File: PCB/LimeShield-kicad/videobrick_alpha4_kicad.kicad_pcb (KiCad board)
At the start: 4 copper layers, 53.2 x 59.6 mm, 91 parts, among them K1 WE-685119134923, Q1 BSS123, Q2 BSS123, Q3 BSS123, Q4 BSS123, U1 ADV7611BSWZ-P, U2 TPS720xx, Y1 CRYSTAL_SMD

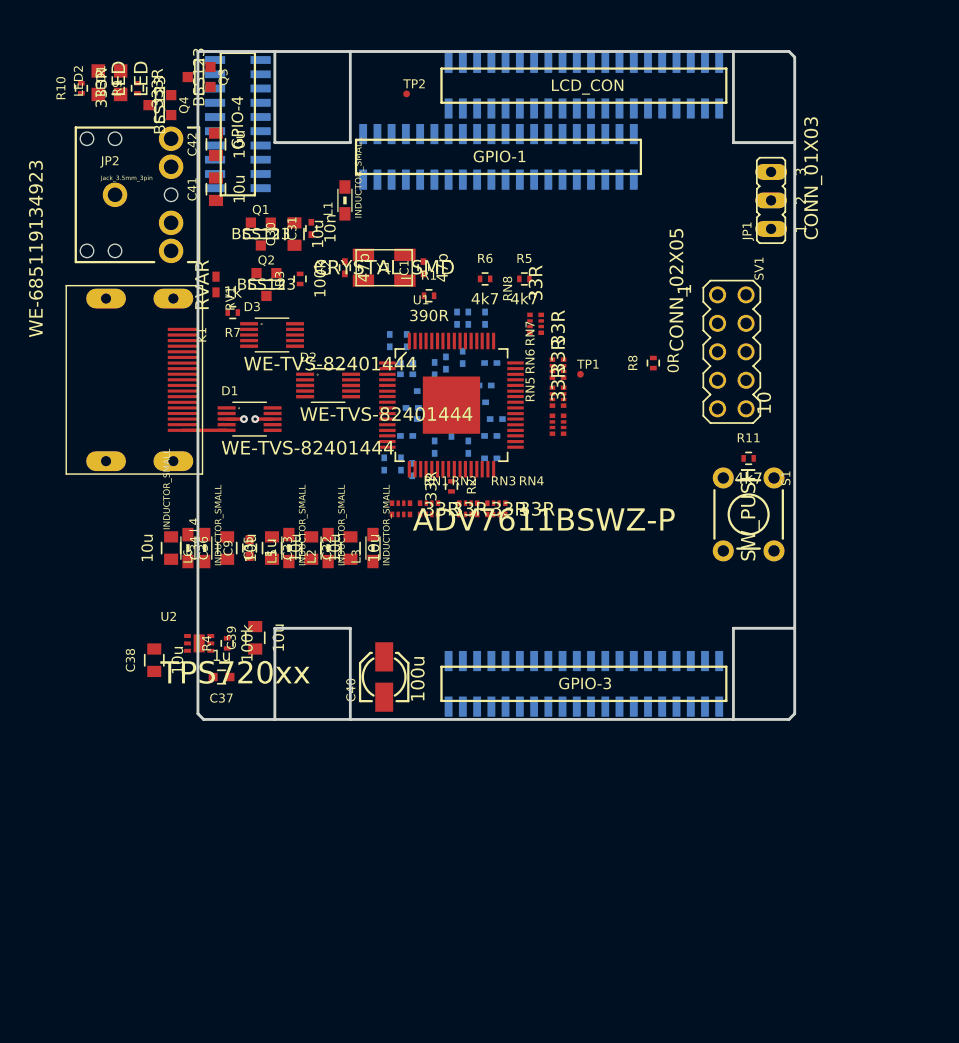
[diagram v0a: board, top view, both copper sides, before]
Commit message: added GPIO-2 on PCB, most things are unrouted, finished conversion from eagle
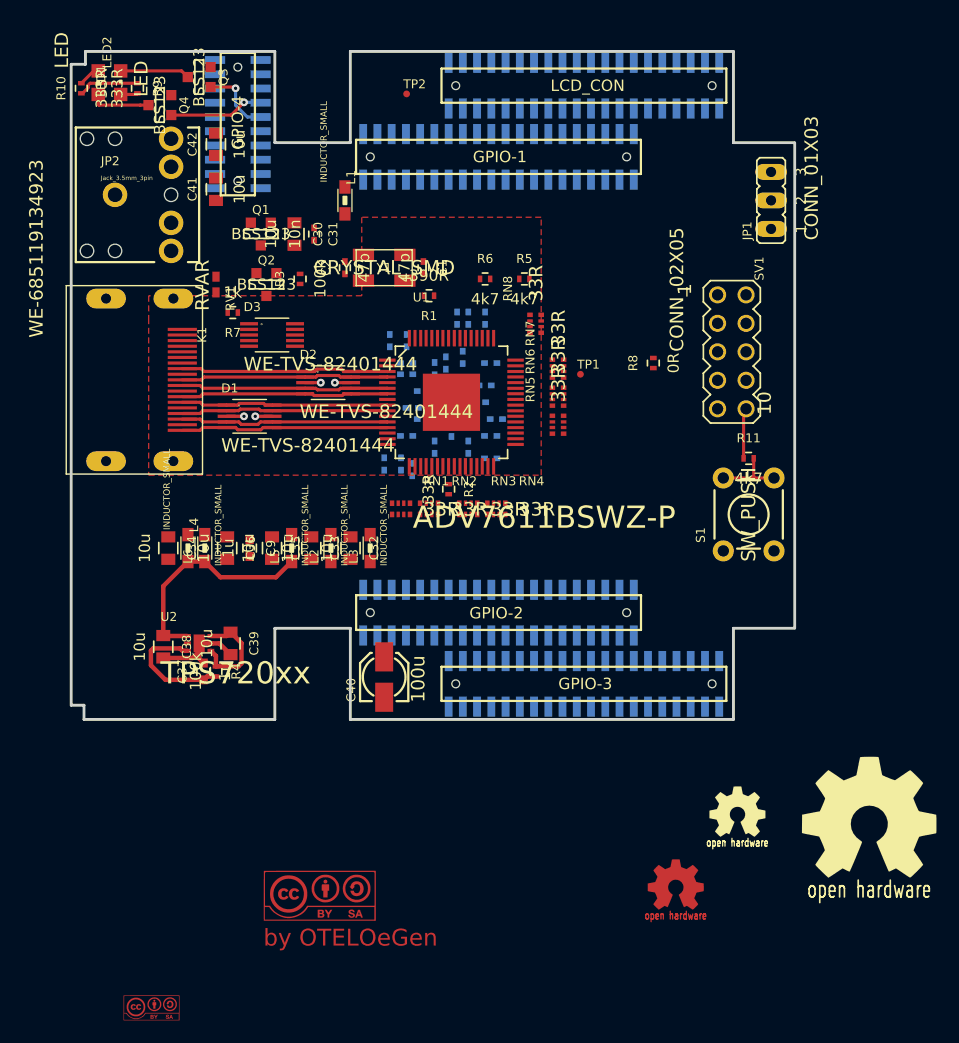
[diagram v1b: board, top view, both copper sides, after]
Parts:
- added G***: LOGO, w_logo:Logo_silk_OSHW_12x13mm, F.Cu at (33.2, 38.5)
- added G***: LOGO, w_logo:Logo_silk_OSHW_6x6mm, F.Cu at (21.5, 38.0)
- added G***: LOGO, w_logo:Logo_copper_OSHW_6x6mm, F.Cu at (16.0, 44.5)
- added G***: LOGO, w_logo:Logo_copper_CC-BY-SA_10x4.5mm, F.Cu at (-15.8, 45.5)
- added G***: LOGO, w_logo:Logo_copper_CC-BY-SA_5x2mm, F.Cu at (-30.8, 55.5)
- added LCD_CON1: FL40YA-V36P-2X20-LF, lime-shield-connector:A10_OLIMEXINO_LIME_SHIELD_1-YA-V36P-2X20-LF, B.Cu at (0.19, 20.3)
- GPIO-1, GPIO-3: footprint A10_OLIMEXINO_LIME_SHIELD_1-YA-V36P-2X20-LF -> lime-shield-connector:A10_OLIMEXINO_LIME_SHIELD_1-YA-V36P-2X20-LF
- GPIO-4: footprint A10_OLIMEXINO_LIME_SHIELD_1-YA-V36P-2X10-LF -> lime-shield-connector:A10_OLIMEXINO_LIME_SHIELD_1-YA-V36P-2X10-LF
- moved R4 2.69 mm to (-25.0, 25.5), turned to 270 degrees
- moved C39 2.26 mm to (-23.7, 23.0), turned to 270 degrees
- moved C37 1.68 mm to (-26.1, 25.5), turned to 90 degrees
- moved C38 1.44 mm to (-29.7, 23.3), turned to 270 degrees
- moved C31 0.56 mm to (-16.2, -13.5), turned to 270 degrees
- moved R2 0.35 mm to (-4.25, 9.25)
- moved C34 0.25 mm to (-29.2, 14.5)
- moved D1 0.25 mm to (-22.0, 2.75)
- moved D2 0.25 mm to (-15.0, -0.25)
- moved L2 0.25 mm to (-14.8, 14.5)
- moved L3 0.25 mm to (-11.2, 14.5)
- moved L5 0.25 mm to (-18.2, 14.5)
- moved U1 0.25 mm to (-4.00, 1.50)
- turned C1 to 270 degrees
- turned C30 to 270 degrees
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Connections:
- C41 pad 2: LINEINR -> LINEINL
- C42 pad 2: LINEINL -> LINEINR
- LCD_CON1 pad 35: (no net) -> /Connectors/CSI1_D8
- U2 pad 3: (no net) -> Net-(C37-Pad1)
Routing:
- net +3.3V: track 1.80 -> 22.3 mm, vias 1 -> 2
- net VDD_1V8: track 0.00 -> 20.1 mm
- net Net-(D1-Pad4): track 0.00 -> 18.6 mm
- net Net-(D2-Pad1): track 0.00 -> 18.6 mm
- net Net-(D2-Pad5): track 0.00 -> 18.5 mm
- net Net-(D1-Pad1): track 0.00 -> 18.5 mm
- net Net-(D1-Pad2): track 0.00 -> 18.5 mm
- net Net-(D2-Pad2): track 0.00 -> 18.5 mm
- net Net-(D2-Pad4): track 0.00 -> 18.5 mm
- net Net-(D1-Pad5): track 3.95 -> 18.6 mm
- net Net-(C37-Pad1): track 0.00 -> 11.2 mm
- net GND: track 1.80 -> 12.5 mm, vias 1 -> 2
- net /Connectors/GPIO3: track 0.00 -> 8.45 mm, vias 0 -> 1
- net /Connectors/GPIO2: track 0.00 -> 6.46 mm, vias 0 -> 1
- net /Connectors/PB2/PWM0: track 0.00 -> 6.27 mm
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- added copper zone on F.Cu, net GND
- added copper zone on In1.Cu, net GND
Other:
- board size 53.2 x 59.6 mm -> 64.5 x 59.6 mm
- net class Default: clearance 0.2 -> 0.15; trace_width 0.3 -> 0.28
- rule trace_clearance: 0.2 -> 0.15
- board text added: "GPIO-2"
- board text added: "by OTELOeGen"
